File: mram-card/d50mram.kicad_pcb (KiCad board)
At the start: 2 copper layers, 86 x 54 mm, 44 parts, among them J1 D50-EDGECONN, SW1 SPDT, SW2 SP4T, SW3 SP4T, U1 EST-MR2A08A, U2 MIC5265-3.3YD5, U3 74LVX541, U4 74LVX541, U5 74LVX541, U6 74LVX4245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

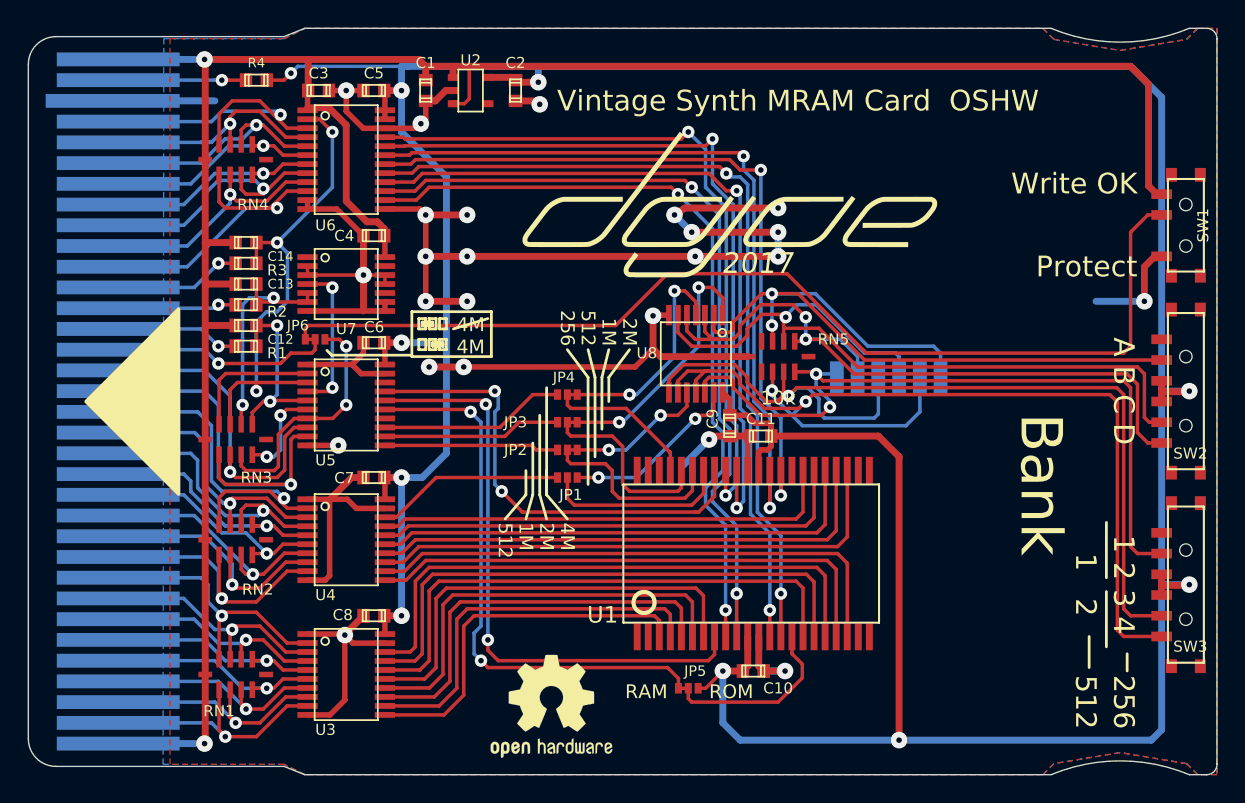
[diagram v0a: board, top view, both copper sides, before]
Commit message: Update to KiCad 6, add Mouser part numbers
Also add a note stating that MIC5245 is a valid replacement
for the MIC5265.

Thanks to @HSBallina for all the parts sleuthing!

Closes #4.
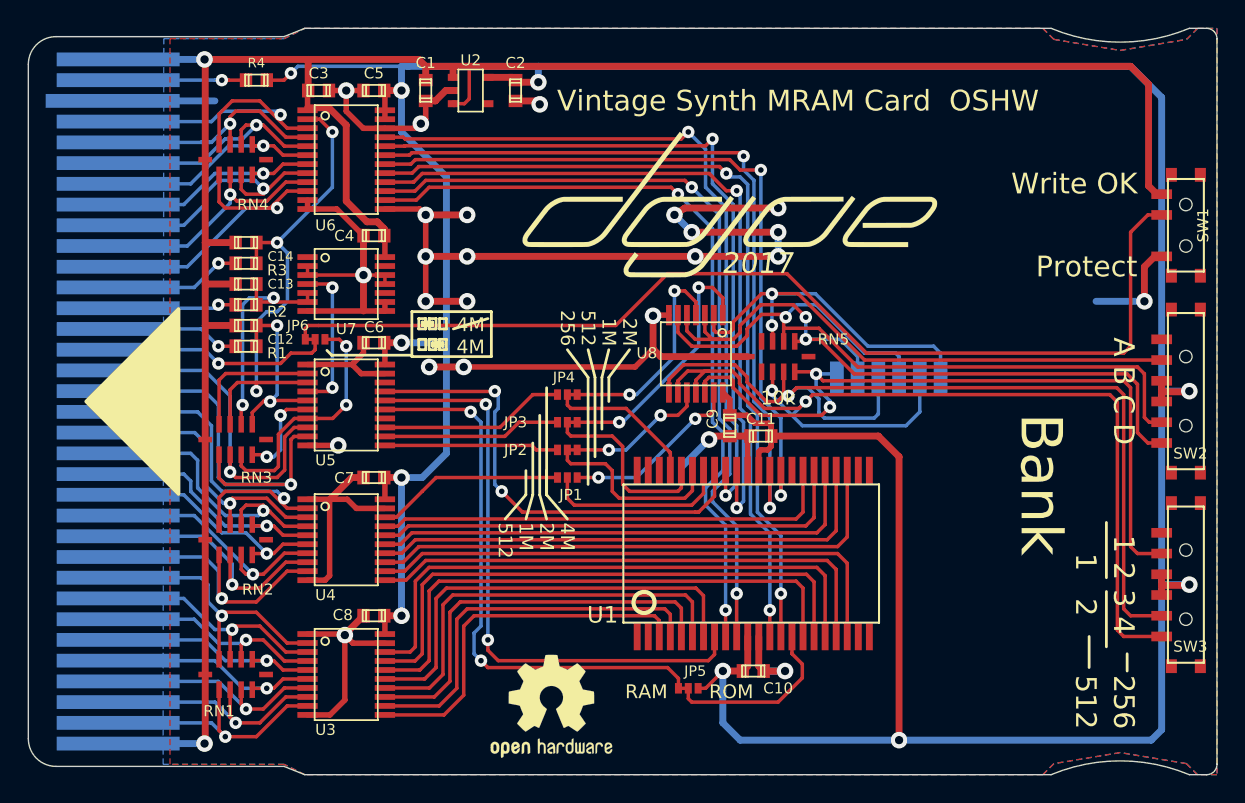
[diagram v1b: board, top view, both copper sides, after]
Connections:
- net /~CEC renamed /~{CEC}
- net /~CEM renamed /~{CEM}
- net /~OEC renamed /~{OEC}
- net /~OEM renamed /~{OEM}
- net /~WEC renamed /~{WEC}
- net /~WEM renamed /~{WEM}
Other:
- outline, holes or cut-outs redrawn
- net class Default removed
- net class Power removed
